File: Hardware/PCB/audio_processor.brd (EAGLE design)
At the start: 100.8 x 61.6 mm, 33 parts, among them IC1 ADS7042DCU, IC2 ADS7042DCU, J1 TMS-101-51-G-D, J10 TMS-101-51-G-D, J11 MTMM-101-X-X-S-X, J12 TMS-101-51-G-D, J2 MTMM-101-X-X-S-X, J3 TMS-101-51-G-D, J4 MTMM-101-X-X-S-X, J5 MTMM-101-X-X-S-X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

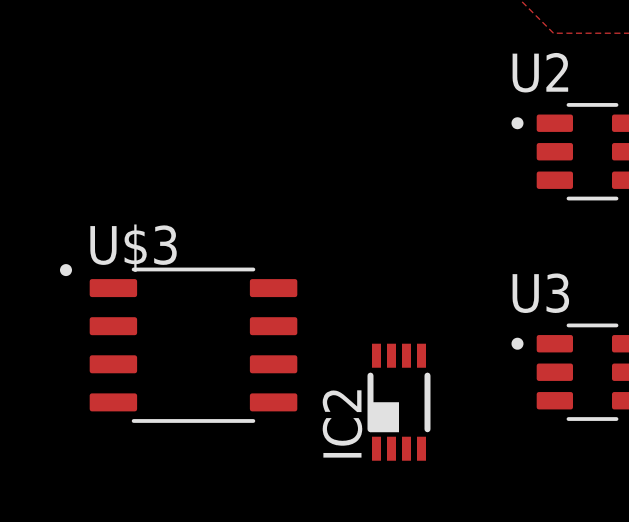
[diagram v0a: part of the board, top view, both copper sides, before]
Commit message: AP_0_02
More README detail.
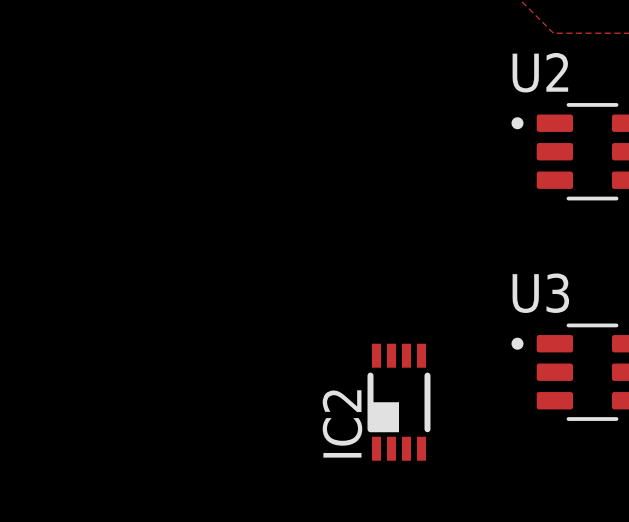
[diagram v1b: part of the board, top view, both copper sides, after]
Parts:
- removed U$3: MCP4822-E/SN, MCP4822-E_SN:SOIC127P599X175-8N
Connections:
- new net N$28: U$1.2, U$2.2
- net N$21: now also U$1.3
- net N$24: now also U$1.4
- net VDD: no longer U$3.1
- net VSS: no longer U$3.7
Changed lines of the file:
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@@
 <attribute name="VALUE" x="-5.5" y="-17.1" size="1.27" layer="27" rot="R90"/>
-</element>
-<element name="U$3" library="MCP4822-E_SN" package="SOIC127P599X175-8N" value="MCP4822-E/SN" x="-14.85" y="-13.2" smashed="yes">
-<attribute name="AVAILABILITY" value="In Stock" x="-14.85" y="-13.2" size="1.778" layer="27" display="off"/>
-<attribute name="CHECK_PRICES" value="https://www.snapeda.com/parts/MCP4822-E/SN/Microchip/view-part/?ref=eda" x="-14.85" y="-13.2" size="1.778" layer="27" display="off"/>
-<attribute name="DESCRIPTION" value="                                                      Dual 12-Bit Dac With Spi Interace And Internal Vref, Soic-8 | Microchip Technology Inc. MCP4822-E/SN                                              " x="-14.85" y="-13.2" size="1.778" layer="27" display="off"/>
-<attribute name="MF" value="Microchip" x="-14.85" y="-13.2" size="1.778" layer="27" display="off"/>
-<attribute name="MP" value="MCP4822-E/SN" x="-14.85" y="-13.2" size="1.778" layer="27" display="off"/>
-<attribute name="NAME" x="-18.425" y="-10.498" size="1.27" layer="25"/>
-<attribute name="PACKAGE" value="SO-8 Microchip" x="-14.85" y="-13.2" size="1.778" layer="27" display="off"/>
-<attribute name="PRICE" value="None" x="-14.85" y="-13.2" size="1.778" layer="27" display="off"/>
-<attribute name="SNAPEDA_LINK" value="https://www.snapeda.com/parts/MCP4822-E/SN/Microchip/view-part/?ref=snap" x="-14.85" y="-13.2" size="1.778" layer="27" display="off"/>
-<attribute name="VALUE" x="-18.425" y="-15.902" size="1.27" layer="27" align="top-left"/>
 </element>
 </elements>
@@
 <signal name="VDD">
 <contactref element="U$1" pad="1"/>
-<contactref element="U$3" pad="1"/>
-<wire x1="-17.52" y1="-11.295" x2="9.43" y2="49.205" width="0" layer="19" extent="1-1"/>
 </signal>
 <signal name="VSS">
 <contactref element="U$1" pad="7"/>
-<contactref element="U$3" pad="7"/>
-<wire x1="-12.18" y1="-12.565" x2="14.77" y2="47.935" width="0" layer="19" extent="1-1"/>
 </signal>
 <signal name="N$21">
@@
 <contactref element="IC2" pad="2"/>
 <contactref element="U$2" pad="6"/>
+<contactref element="U$1" pad="3"/>
 <wire x1="43.12" y1="56.07" x2="83.15" y2="49.4" width="0" layer="19" extent="1-1"/>
-<wire x1="-8.25" y1="-16.65" x2="43.12" y2="56.07" width="0" layer="19" extent="1-1"/>
+<wire x1="9.43" y1="46.665" x2="43.12" y2="56.07" width="0" layer="19" extent="1-1"/>
+<wire x1="-8.25" y1="-16.65" x2="9.43" y2="46.665" width="0" layer="19" extent="1-1"/>
 </signal>
 <signal name="V+">
@@
 <contactref element="IC1" pad="3"/>
 <contactref element="U$2" pad="5"/>
+<contactref element="U$1" pad="4"/>
 <wire x1="45.66" y1="56.07" x2="83.65" y2="49.4" width="0" layer="19" extent="1-1"/>
-<wire x1="-7.75" y1="-16.65" x2="45.66" y2="56.07" width="0" layer="19" extent="1-1"/>
+<wire x1="9.43" y1="45.395" x2="45.66" y2="56.07" width="0" layer="19" extent="1-1"/>
+<wire x1="-7.75" y1="-16.65" x2="9.43" y2="45.395" width="0" layer="19" extent="1-1"/>
 </signal>
 <signal name="N$25">
@@
 <wire x1="-7.25" y1="-16.65" x2="50.74" y2="56.07" width="0" layer="19" extent="1-1"/>
 </signal>
+<signal name="N$28">
+<contactref element="U$1" pad="2"/>
+<contactref element="U$2" pad="2"/>
+<wire x1="9.43" y1="47.935" x2="53.28" y2="56.07" width="0" layer="19" extent="1-1"/>
+</signal>
 </signals>

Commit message: AP_0_03
First public commit.  Uses timer group (as opposed to GPTimer).
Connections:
- new net N$20: U$1.5, U$2.4
- net N$21: now also U$2.9; no longer U$2.6
- net N$24: now also U$2.10; no longer U$2.5
- net N$25: now also U$2.2; no longer U$2.4
- net N$26: now also U$2.1; no longer U$2.3
- net N$28: now also U$2.3; no longer U$2.2
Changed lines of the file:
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@@
 <contactref element="IC1" pad="2"/>
 <contactref element="IC2" pad="2"/>
-<contactref element="U$2" pad="6"/>
 <contactref element="U$1" pad="3"/>
-<wire x1="43.12" y1="56.07" x2="83.15" y2="49.4" width="0" layer="19" extent="1-1"/>
-<wire x1="9.43" y1="46.665" x2="43.12" y2="56.07" width="0" layer="19" extent="1-1"/>
+<contactref element="U$2" pad="9"/>
+<wire x1="43.12" y1="40.83" x2="83.15" y2="49.4" width="0" layer="19" extent="1-1"/>
+<wire x1="9.43" y1="46.665" x2="43.12" y2="40.83" width="0" layer="19" extent="1-1"/>
 <wire x1="-8.25" y1="-16.65" x2="9.43" y2="46.665" width="0" layer="19" extent="1-1"/>
 </signal>
@@
 <contactref element="IC2" pad="3"/>
 <contactref element="IC1" pad="3"/>
-<contactref element="U$2" pad="5"/>
 <contactref element="U$1" pad="4"/>
-<wire x1="45.66" y1="56.07" x2="83.65" y2="49.4" width="0" layer="19" extent="1-1"/>
-<wire x1="9.43" y1="45.395" x2="45.66" y2="56.07" width="0" layer="19" extent="1-1"/>
+<contactref element="U$2" pad="10"/>
+<wire x1="45.66" y1="40.83" x2="83.65" y2="49.4" width="0" layer="19" extent="1-1"/>
+<wire x1="9.43" y1="45.395" x2="45.66" y2="40.83" width="0" layer="19" extent="1-1"/>
 <wire x1="-7.75" y1="-16.65" x2="9.43" y2="45.395" width="0" layer="19" extent="1-1"/>
 </signal>
 <signal name="N$25">
 <contactref element="IC1" pad="4"/>
-<contactref element="U$2" pad="4"/>
-<wire x1="48.2" y1="56.07" x2="84.15" y2="49.4" width="0" layer="19" extent="1-1"/>
+<contactref element="U$2" pad="2"/>
+<wire x1="53.28" y1="56.07" x2="84.15" y2="49.4" width="0" layer="19" extent="1-1"/>
 </signal>
 <signal name="N$26">
 <contactref element="IC2" pad="4"/>
-<contactref element="U$2" pad="3"/>
-<wire x1="-7.25" y1="-16.65" x2="50.74" y2="56.07" width="0" layer="19" extent="1-1"/>
+<contactref element="U$2" pad="1"/>
+<wire x1="-7.25" y1="-16.65" x2="55.82" y2="56.07" width="0" layer="19" extent="1-1"/>
 </signal>
 <signal name="N$28">
 <contactref element="U$1" pad="2"/>
-<contactref element="U$2" pad="2"/>
-<wire x1="9.43" y1="47.935" x2="53.28" y2="56.07" width="0" layer="19" extent="1-1"/>
+<contactref element="U$2" pad="3"/>
+<wire x1="9.43" y1="47.935" x2="50.74" y2="56.07" width="0" layer="19" extent="1-1"/>
+</signal>
+<signal name="N$20">
+<contactref element="U$1" pad="5"/>
+<contactref element="U$2" pad="4"/>
+<wire x1="14.77" y1="45.395" x2="48.2" y2="56.07" width="0" layer="19" extent="1-1"/>
 </signal>
 </signals>

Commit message: AP_0_05
Updated README.
Barrel connector library added.
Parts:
- added J9: PJ-102AH, PJ-102AH:CUI_PJ-102AH
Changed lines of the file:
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@@
 <attribute name="VALUE" x="-5.5" y="-17.1" size="1.27" layer="27" rot="R90"/>
+</element>
+<element name="J9" library="PJ-102AH" package="CUI_PJ-102AH" value="PJ-102AH" x="-2.55" y="-25.6" smashed="yes">
+<attribute name="AVAILABILITY" value="In Stock" x="-2.55" y="-25.6" size="1.778" layer="27" display="off"/>
+<attribute name="CHECK_PRICES" value="https://www.snapeda.com/parts/PJ-102AH/Same+Sky/view-part/?ref=eda" x="-2.55" y="-25.6" size="1.778" layer="27" display="off"/>
+<attribute name="DESCRIPTION" value="                                                      2.0 x 6.5 mm, 5.0 A, Horizontal, Through Hole, Tapered Pins, Dc Power Jack Connector                                              " x="-2.55" y="-25.6" size="1.778" layer="27" display="off"/>
+<attribute name="MF" value="Same Sky" x="-2.55" y="-25.6" size="1.778" layer="27" display="off"/>
+<attribute name="MP" value="PJ-102AH" x="-2.55" y="-25.6" size="1.778" layer="27" display="off"/>
+<attribute name="NAME" x="-9.748709375" y="-19.46258125" size="1.271540625" layer="25"/>
+<attribute name="PACKAGE" value="None" x="-2.55" y="-25.6" size="1.778" layer="27" display="off"/>
+<attribute name="PRICE" value="None" x="-2.55" y="-25.6" size="1.778" layer="27" display="off"/>
+<attribute name="SNAPEDA_LINK" value="https://www.snapeda.com/parts/PJ-102AH/Same+Sky/view-part/?ref=snap" x="-2.55" y="-25.6" size="1.778" layer="27" display="off"/>
+<attribute name="VALUE" x="-9.7469" y="-32.01615" size="1.27121875" layer="27"/>
 </element>
 </elements>
